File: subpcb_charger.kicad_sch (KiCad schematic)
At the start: 28 parts, among them J10 Screw_Terminal_01x02, J17 Conn_01x02, J19 Conn_01x02, J27 Conn_01x05, J3 Screw_Terminal_01x03, J56 Screw_Terminal_01x02, J57 Conn_01x02, J58 Screw_Terminal_01x02, J59 Conn_01x02, J60 Screw_Terminal_01x02, J61 Conn_01x02, J62 Screw_Terminal_01x02, J63 Conn_01x02, J9 Conn_01x02, U14 Fuse Holder, U15 Fuse Holder, U16 Fuse Holder, U17 Fuse Holder, U72 Jumper Red, U73 Jumper Blue

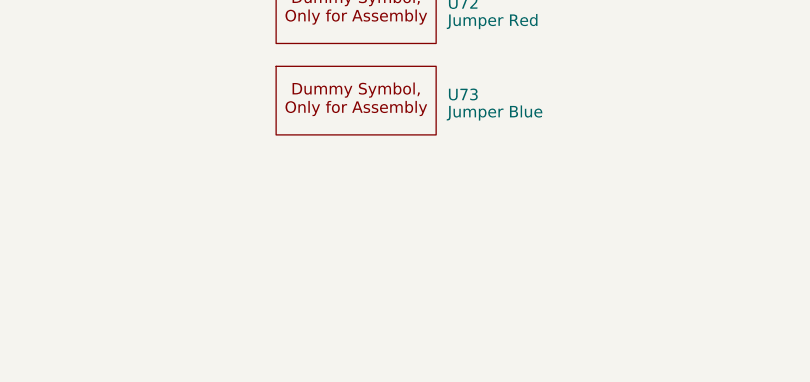
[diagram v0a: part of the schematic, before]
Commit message: Added Fuse
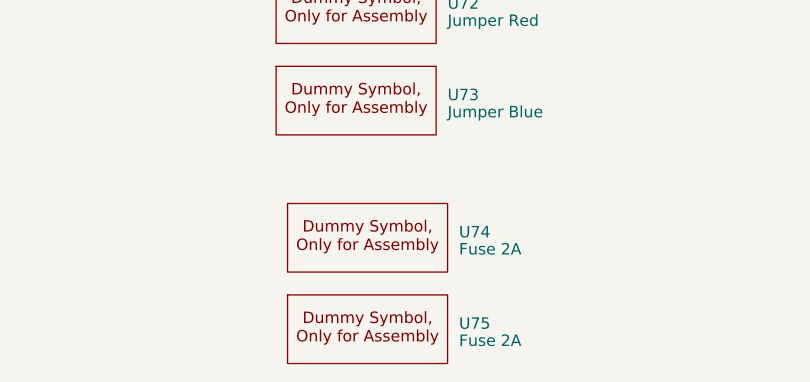
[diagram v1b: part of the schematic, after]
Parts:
- added U74, U75: Fuse 2A, xtech:Dummy, symbol xtech:Dummy
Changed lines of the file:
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@@
 	)
 	(symbol
+		(lib_id "xtech:Dummy")
+		(at 254 207.01 0)
+		(unit 1)
+		(exclude_from_sim no)
+		(in_bom yes)
+		(on_board yes)
+		(dnp no)
+		(fields_autoplaced yes)
+		(property "Reference" "U74"
+			(at 273.05 202.5649 0)
+			(effects
+				(font
+					(size 1.27 1.27)
+				)
+				(justify left)
+			)
+		)
+		(property "Value" "Fuse 2A"
+			(at 273.05 204.47 0)
+			(effects
+				(font
+					(size 1.27 1.27)
+				)
+				(justify left)
+			)
+		)
+		(property "Footprint" "xtech:Dummy"
+			(at 254 207.01 0)
+			(effects
+				(font
+					(size 1.27 1.27)
+				)
+				(hide yes)
+			)
+		)
+		(property "Datasheet" ""
+			(at 254 207.01 0)
+			(effects
+				(font
+					(size 1.27 1.27)
+				)
+				(hide yes)
+			)
+		)
+		(property "Description" ""
+			(at 254 207.01 0)
+			(effects
+				(font
+					(size 1.27 1.27)
+				)
+				(hide yes)
+			)
+		)
+		(property "JLC" "C356459"
+			(at 254 207.01 0)
+			(effects
+				(font
+					(size 1.27 1.27)
+				)
+				(hide yes)
+			)
+		)
+		(instances
+			(project "hw-openmower-universal"
+				(path "/e12e8a63-1d1b-4736-9aba-a87a258b2b11/2930b75f-7142-4414-b99a-728851a6a7da"
+					(reference "U74")
+					(unit 1)
+				)
+			)
+		)
+	)
+	(symbol
 		(lib_id "Device:D_Zener")
 		(at 104.14 59.69 270)
@@
 					(unit 1)
 				)
+			)
+		)
+	)
+	(symbol
+		(lib_id "xtech:Dummy")
+		(at 254 217.17 0)
+		(unit 1)
+		(exclude_from_sim no)
+		(in_bom yes)
+		(on_board yes)
+		(dnp no)
+		(fields_autoplaced yes)
+		(property "Reference" "U75"
+			(at 273.05 212.7249 0)
+			(effects
+				(font
+					(size 1.27 1.27)
+				)
+				(justify left)
+			)
+		)
+		(property "Value" "Fuse 2A"
+			(at 273.05 214.63 0)
+			(effects
+				(font
+					(size 1.27 1.27)
+				)
+				(justify left)
+			)
+		)
+		(property "Footprint" "xtech:Dummy"
+			(at 254 217.17 0)
+			(effects
+				(font
+					(size 1.27 1.27)
+				)
+				(hide yes)
+			)
+		)
+		(property "Datasheet" ""
+			(at 254 217.17 0)
+			(effects
+				(font
+					(size 1.27 1.27)
+				)
+				(hide yes)
+			)
+		)
+		(property "Description" ""
+			(at 254 217.17 0)
+			(effects
+				(font
+					(size 1.27 1.27)
+				)
+				(hide yes)
+			)
+		)
+		(property "JLC" "C356459"
+			(at 254 217.17 0)
+			(effects
+				(font
+					(size 1.27 1.27)
+				)
+				(hide yes)
+			)
+		)
+		(instances
+			(project "hw-openmower-universal"
+				(path "/e12e8a63-1d1b-4736-9aba-a87a258b2b11/2930b75f-7142-4414-b99a-728851a6a7da"
+					(reference "U75")
+					(unit 1)
+				)

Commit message: Fixed BOM
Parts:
- J27: JLC (none) -> C157991
